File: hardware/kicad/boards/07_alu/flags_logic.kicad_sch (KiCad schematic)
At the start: 53 parts, among them J6 Conn_02x07_Odd_Even, U1 74LS377, U10 74LS32, U11 74LS30, U12 74LS30, U13 74LS540, U14 74LS540, U2 74LS377, U3 74LS540, U4 74HC86, U5 74LS08, U6 74LS30, U7 74LS30, U8 74LS540, U9 74LS540

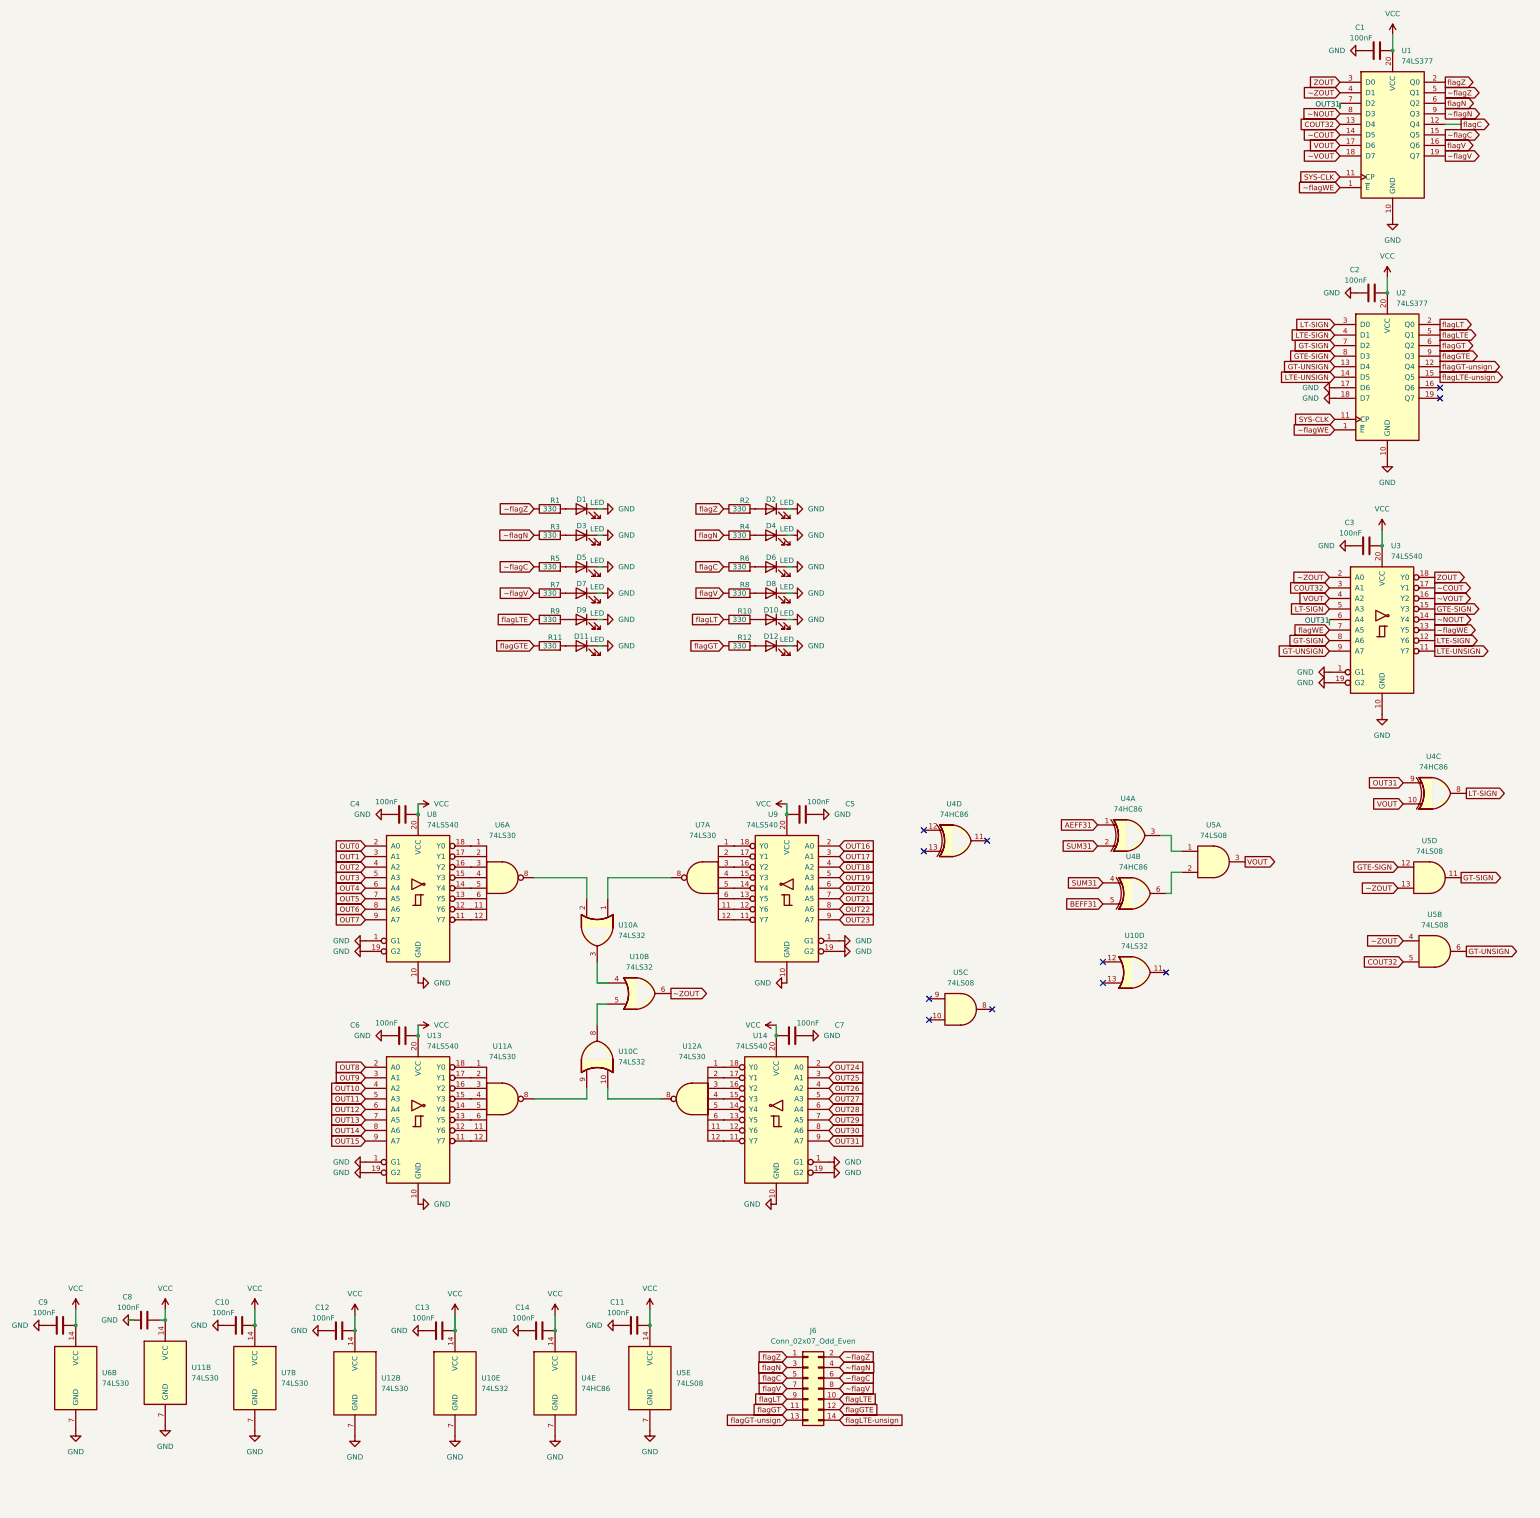
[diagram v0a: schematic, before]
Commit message: feat: implemented flag logic and led for 16 alu; refactored alu-1b cells
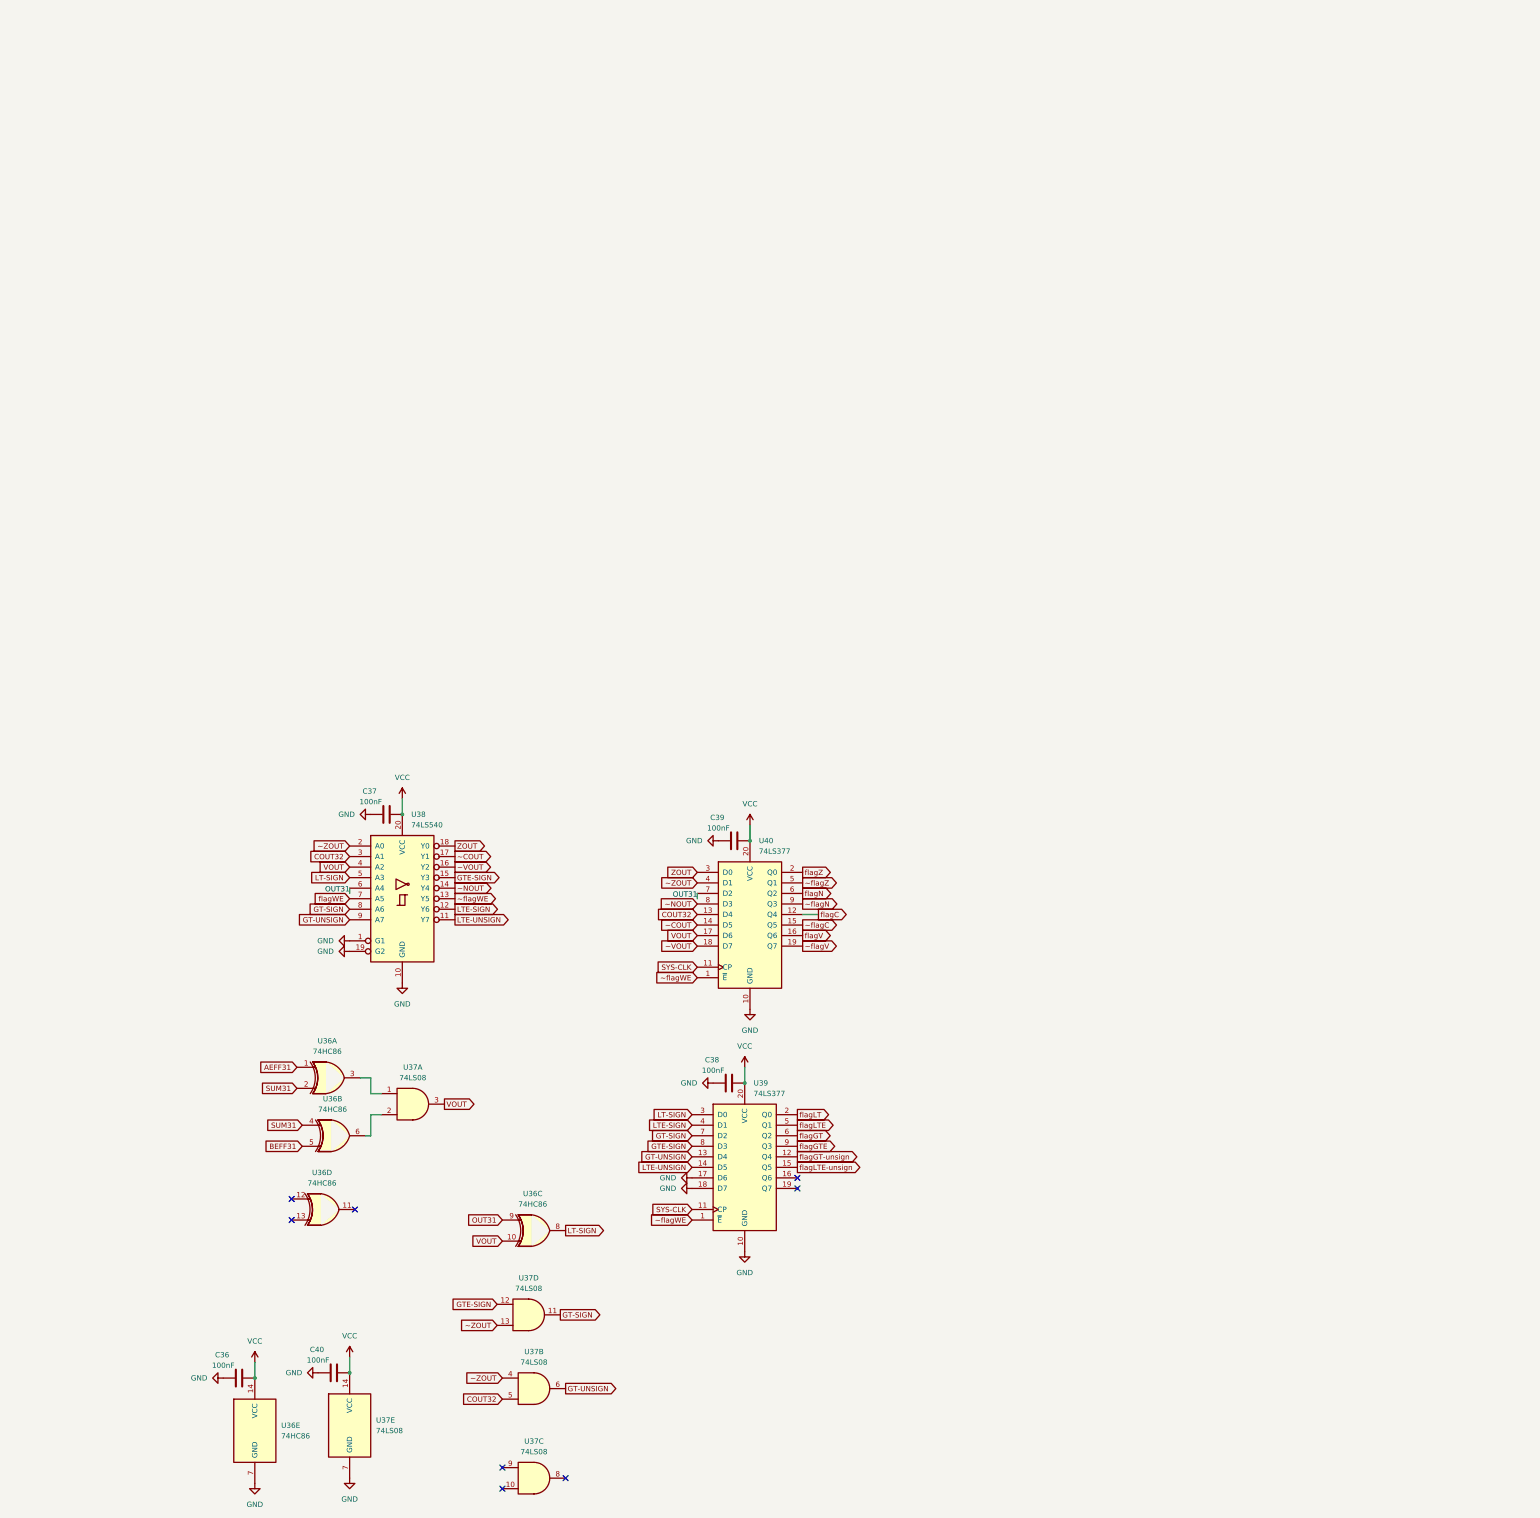
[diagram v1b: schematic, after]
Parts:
- removed C1, C10, C11, C12, C13, C14, C2, C3, C4, C5, C6, C7, C8, C9: 100nF, Capacitor_SMD:C_0603_1608Metric, symbol Device:C
- removed D1, D10, D11, D12, D2, D3, D4, D5, D6, D7, D8, D9: LED, LED_SMD:LED_0805_2012Metric, symbol Device:LED
- removed J6: Conn_02x07_Odd_Even, Connector_PinHeader_2.54mm:PinHeader_2x07_P2.54mm_Vertical, symbol Connector_Generic:Conn_02x07_Odd_Even
- removed R1, R10, R11, R12, R2, R3, R4, R5, R6, R7, R8, R9: 330, Resistor_SMD:R_0603_1608Metric, symbol Device:R
- removed U1, U2: 74LS377, Package_SO:SOIC-20W_7.5x12.8mm_P1.27mm, symbol 74xx:74LS377
- removed U10: 74LS32, Package_SO:SOIC-14_3.9x8.7mm_P1.27mm, symbol 74xx:74LS32
- removed U11, U12, U6, U7: 74LS30, Package_SO:SOIC-14_3.9x8.7mm_P1.27mm, symbol 74xx:74LS30
- removed U13, U14, U3, U8, U9: 74LS540, Package_SO:SOIC-20W_7.5x12.8mm_P1.27mm, symbol 74xx:74LS540
- removed U4: 74HC86, Package_SO:SOIC-14_3.9x8.7mm_P1.27mm, symbol 74xx:74HC86
- removed U5: 74LS08, Package_SO:SOIC-14_3.9x8.7mm_P1.27mm, symbol 74xx:74LS08
- added C36, C37, C38, C39, C40: 100nF, Capacitor_SMD:C_0603_1608Metric, symbol Device:C
- added U36: 74HC86, Package_SO:SOIC-14_3.9x8.7mm_P1.27mm, symbol 74xx:74HC86
- added U37: 74LS08, Package_SO:SOIC-14_3.9x8.7mm_P1.27mm, symbol 74xx:74LS08
- added U38: 74LS540, Package_SO:SOIC-20W_7.5x12.8mm_P1.27mm, symbol 74xx:74LS540
- added U39, U40: 74LS377, Package_SO:SOIC-20W_7.5x12.8mm_P1.27mm, symbol 74xx:74LS377
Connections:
- net AEFF31: now also U36.1
- net BEFF31: now also U36.5
- net COUT32: now also U37.5, U38.3 (A1), U40.13 (D4)
- net GND: now also C36.1, C37.1, C38.1, C39.1, C40.1, U36.7 (GND), U37.7 (GND), U38.1 (G1), U38.10 (GND), U38.19 (G2), U39.10 (GND), U39.17 (D6), U39.18 (D7), U40.10 (GND)
- net GT-SIGN: now also U37.11, U38.8 (A6), U39.7 (D2)
- net GT-UNSIGN: now also U37.6, U38.9 (A7), U39.13 (D4)
- net GTE-SIGN: now also U37.12, U38.15 (Y3), U39.8 (D3)
- net LT-SIGN: now also U36.8, U38.5 (A3), U39.3 (D0)
- net LTE-SIGN: now also U38.12 (Y6), U39.4 (D1)
- net LTE-UNSIGN: now also U38.11 (Y7), U39.14 (D5)
- net OUT31: now also U36.9, U38.6 (A4), U40.7 (D2)
- net SUM31: now also U36.2, U36.4
- net SYS-CLK: now also U39.11 (CP), U40.11 (CP)
- net VCC: now also C36.2, C37.2, C38.2, C39.2, C40.2, U36.14 (VCC), U37.14 (VCC), U38.20 (VCC), U39.20 (VCC), U40.20 (VCC)
- net VOUT: now also U36.10, U37.3, U38.4 (A2), U40.17 (D6)
- net ZOUT: now also U38.18 (Y0), U40.3 (D0)
- net flagC: now also U40.12 (Q4)
- net flagGT: now also U39.6 (Q2)
- net flagGT-unsign: now also U39.12 (Q4)
- net flagGTE: now also U39.9 (Q3)
- net flagLT: now also U39.2 (Q0)
- net flagLTE: now also U39.5 (Q1)
- net flagLTE-unsign: now also U39.15 (Q5)
- net flagN: now also U40.6 (Q2)
- net flagV: now also U40.16 (Q6)
- net flagWE: now also U38.7 (A5)
- net flagZ: now also U40.2 (Q0)
- net ~COUT: now also U38.17 (Y1), U40.14 (D5)
- net ~NOUT: now also U38.14 (Y4), U40.8 (D3)
- net ~VOUT: now also U38.16 (Y2), U40.18 (D7)
- net ~ZOUT: now also U37.13, U37.4, U38.2 (A0), U40.4 (D1)
- net ~flagC: now also U40.15 (Q5)
- net ~flagN: now also U40.9 (Q3)
- net ~flagV: now also U40.19 (Q7)
- net ~flagWE: now also U38.13 (Y5), U39.1 (~{E}), U40.1 (~{E})
- net ~flagZ: now also U40.5 (Q1)
- new net: U36.3, U37.1
- new net: U36.6, U37.2
- no-connect marks 11 -> 8

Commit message: checkpoint: most recent 16b cell: ~120mm by 120mm
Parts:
- removed C38: 100nF, Capacitor_SMD:C_0603_1608Metric, symbol Device:C
- removed U39: 74LS377, Package_SO:SOIC-20W_7.5x12.8mm_P1.27mm, symbol 74xx:74LS377
- added C16, C49, C50: 100nF, Capacitor_SMD:C_0603_1608Metric, symbol Device:C
- added U16: 74ACT151, Package_SO:SOIC-16_3.9x9.9mm_P1.27mm, symbol 74xx:74LS151
- added U4, U6: 74HC688, Package_SO:SOIC-20W_7.5x12.8mm_P1.27mm, symbol 74xx:74HC688
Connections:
- net ~flagC is gone; now on net flagLT: U40.15 (Q5)
- net ~flagN is gone; now on net flagC: U40.9 (Q3)
- net ~flagV is gone; now on net flagGTE: U40.19 (Q7)
- net GND: now also C16.1, C49.1, C50.1, U16.4 (I0), U16.7 (~{E}), U16.8 (GND), U4.1 (G), U4.10 (GND), U4.12 (R4), U4.14 (R5), U4.16 (R6), U4.18 (R7), U4.3 (R0), U4.5 (R1), U4.7 (R2), U4.9 (R3), U6.10 (GND), U6.12 (R4), U6.14 (R5), U6.16 (R6), U6.18 (R7), U6.3 (R0), U6.5 (R1), U6.7 (R2), U6.9 (R3)
- net GT-SIGN: now also U40.17 (D6); no longer U38.8 (A6)
- net GTE-SIGN: now also U40.18 (D7)
- net LT-SIGN: now also U40.14 (D5)
- net VCC: now also C16.2, C49.2, C50.2, U16.16 (VCC), U16.3 (I1), U4.20 (VCC), U6.20 (VCC)
- net VOUT: now also U40.13 (D4); no longer U40.17 (D6)
- net flagC: now also U16.2 (I2); no longer U40.12 (Q4)
- net flagGT: now also U40.16 (Q6), U16.12 (I7)
- net flagLT: now also U16.13 (I6)
- net flagN: now also U16.15 (I4)
- net flagV: now also U40.12 (Q4), U16.14 (I5); no longer U40.16 (Q6)
- net flagZ: now also U16.1 (I3)
- net ~ZOUT: now also U6.19 (P=R); no longer U37.4
- net AEFF31 renamed Aeff
- net BEFF31 renamed Beff
- removed net COUT32: U37.5, U38.3 (A1), U40.13 (D4)
- net GT-UNSIGN: no longer names the net of U38.9 (A7)
- net GT-UNSIGN: no longer U37.6
- net LTE-SIGN: no longer names the net of U38.12 (Y6)
- net LTE-UNSIGN: no longer names the net of U38.11 (Y7)
- net OUT31 renamed OUT15
- net OUT15: now also U6.17 (P7)
- net SUM31 renamed sum15
- net flagWE renamed FLAG_WE
- net ~COUT: no longer names the net of U38.17 (Y1)
- net ~COUT: no longer U40.14 (D5)
- net ~NOUT: no longer names the net of U38.14 (Y4)
- net ~NOUT: no longer U40.8 (D3)
- net ~VOUT: no longer names the net of U38.16 (Y2)
- net ~VOUT: no longer U40.18 (D7)
- new net: U4.19 (P=R), U6.1 (G)
- new net CIN-MAIN: U16.5 (Z)
- new net COUT-MAIN: U40.8 (D3)
- new net CSEL0: U16.11 (S0)
- new net CSEL1: U16.10 (S1)
- new net CSEL2: U16.9 (S2)
- new net OUT0: U4.2 (P0)
- new net OUT1: U4.4 (P1)
- new net OUT10: U6.6 (P2)
- new net OUT11: U6.8 (P3)
- new net OUT12: U6.11 (P4)
- new net OUT13: U6.13 (P5)
- new net OUT14: U6.15 (P6)
- new net OUT2: U4.6 (P2)
- new net OUT3: U4.8 (P3)
- new net OUT4: U4.11 (P4)
- new net OUT5: U4.13 (P5)
- new net OUT6: U4.15 (P6)
- new net OUT7: U4.17 (P7)
- new net OUT8: U6.2 (P0)
- new net OUT9: U6.4 (P1)
- no-connect marks 8 -> 18
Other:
- moved on the sheet: C36, C37, C39, C40, U36A, U36B, U36C, U36D, U36E, U37A, U37B, U37C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
